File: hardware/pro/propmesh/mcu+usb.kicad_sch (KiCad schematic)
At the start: 14 parts, among them J4 TYPE-C-31-M-12, SW1 TS-1187A, SW2 TS-1187A, U3 ESP32-S3-WROOM-1U-N8R2, U4 USBLC6-2SC6

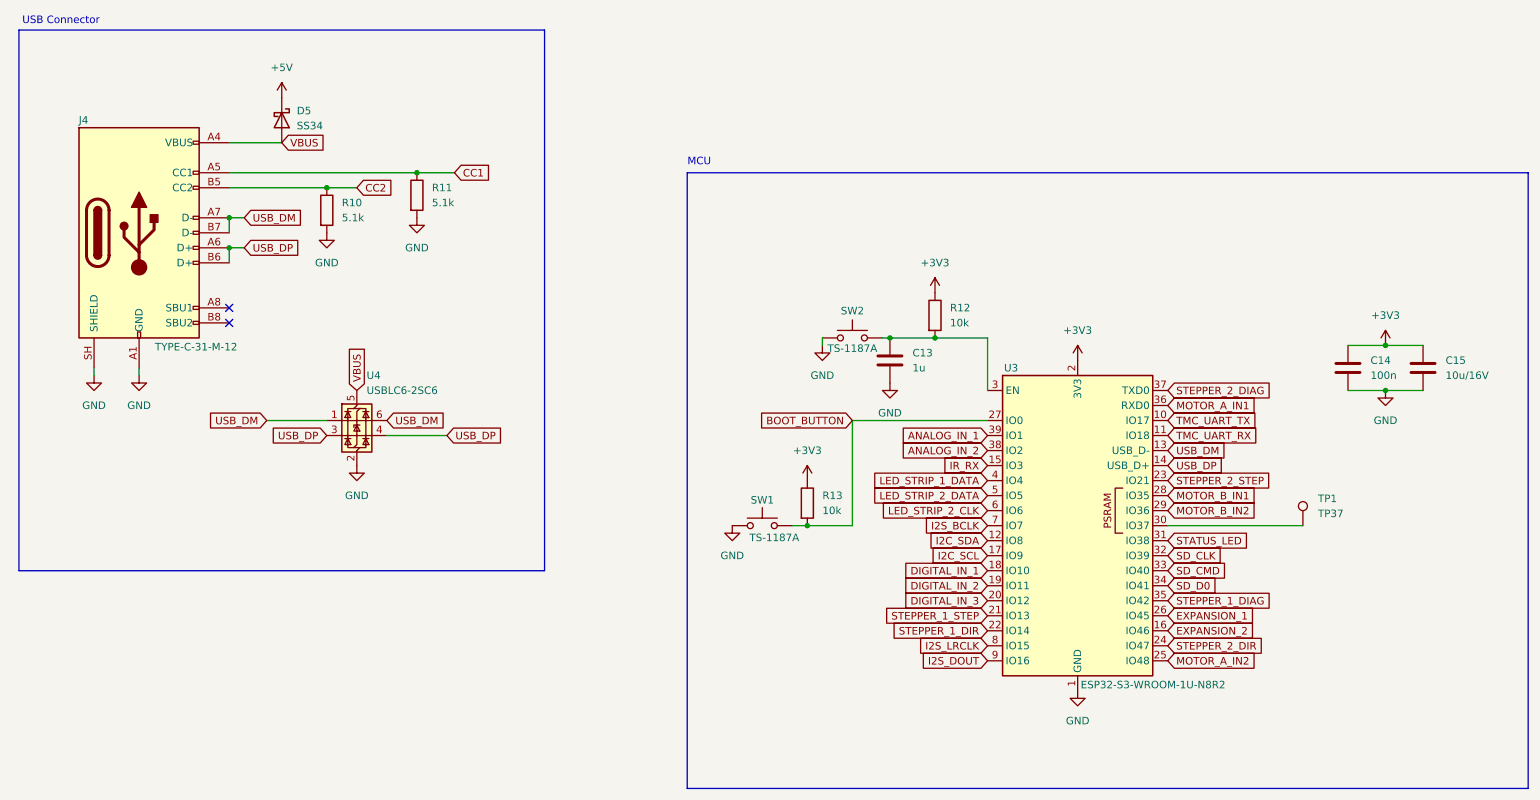
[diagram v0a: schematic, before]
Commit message: Pro schematic complete; enclosure, layout guide, timeline and radio decisions
Schematic: all seven design sheets drawn and green; project-wide ERC at
zero. IR receiver dropped (hidden board can't see a remote — plug-in on
a DIGITAL_IN); GPIO 3 became LED_STRIP_1_CLK; both strip outputs 3- or
4-wire through one octal SN74AHCT541DWR (three revisions of the shifter
in one day, no mode jumpers). Input FET symbol replaced: KiCad 10's
Device:Q_PMOS numbers pins D/G/S and matches no pad — the part would
have been unconnected with no ERC/DRC complaint. All 196 references
renumbered to standard sequential designators (yaml keeps spec names;
the checker prints both). Sheet 08 (test points) and the sheet 01
staged-power link headers specified per spec §2.6 — sheet 01's checker
is red until they are drawn.

checknet.py: symbol pins ⊆ footprint pads check (the silent killer),
multi-unit pin keys + per-unit diagrams (`units:`), symbol-vote sheet
anchoring for half-drawn sheets, orientation-aware net voting, foreign
part reporting, cross-sheet extras no longer crash the report.

Docs: hardware/pro/layout.md — placement by designator, IPC-2221 trace
widths, thermal, silk, ⚠ list, KiCad primer; every chip's datasheet
layout section read (WROOM-1U has NO keep-out; DRV8871 wants a bottom
GND pour; MAX98357A output-trace numbers). Enclosure plan (spec §2.3):
Multilink RNI-1500 / RNI-300, DRiBOX Medium, Joinfworld clear-lid box,
icotek KEL-DPZ entry plate, fit rule 210×140×60 mm inside; PSU
defaults (§2.9) and the 10 A input-path note. Software plan: timeline
design (ramps native, live scrub v1, Cue.start_offset_ms in schema),
yard access (walk-up AP, WireGuard-in-firmware, BYO remote), WiFi-PHY
radio decision vs Zigbee/BLE/LoRa, console served-from-bridge budget,
USB stays in CDC/JTAG mode (no auto-program transistors needed).

Co-Authored-By: Claude Fable 5.1 <noreply@anthropic.com>
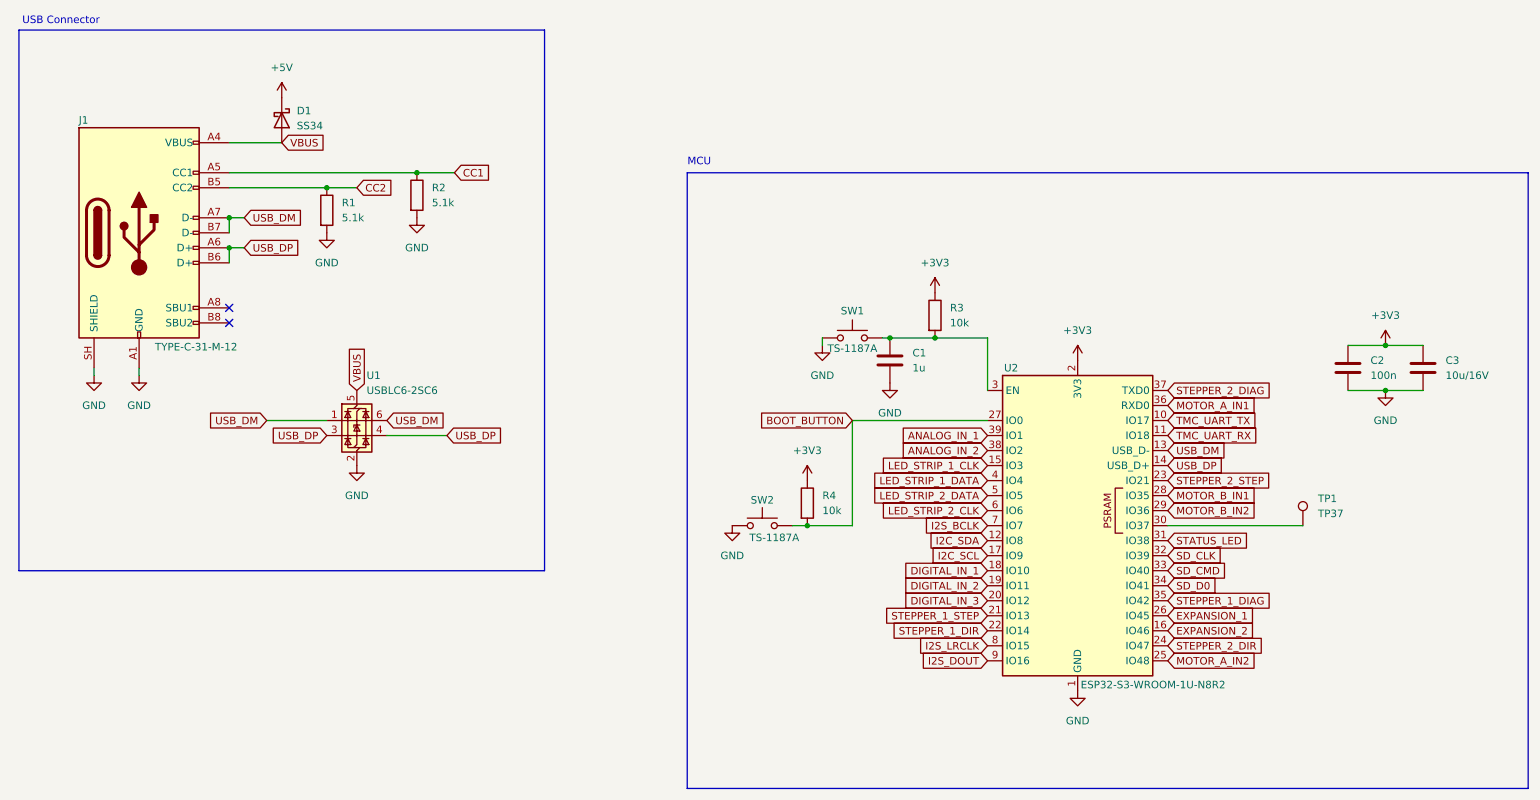
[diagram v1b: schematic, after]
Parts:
- renumbered C13 to C1, C14 to C2, C15 to C3, D5 to D1, J4 to J1, R10 to R1, R11 to R2, R12 to R3, R13 to R4, SW2 to SW1, SW1 to SW2, U4 to U1, U3 to U2
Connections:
- net IR_RX renamed LED_STRIP_1_CLK
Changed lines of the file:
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@@
 		)
 	)
-	(global_label "IR_RX"
+	(global_label "LED_STRIP_1_CLK"
 		(shape input)
 		(at 186.69 93.98 180)
@@
 		)
 		(property "Intersheetrefs" "${INTERSHEET_REFS}"
-			(at 178.3829 93.98 0)
+			(at 167.2554 93.98 0)
 			(hide yes)
 			(show_name no)
@@
 		(dnp no)
 		(fields_autoplaced yes)
-		(property "Reference" "C15"
+		(property "Reference" "C3"
 			(at 264.16 76.1999 0)
 			(show_name no)
@@
 			(project "propmesh"
 				(path "/6aa579d1-bfe0-499b-882d-72f52ff6d36c/0f32bd3b-d69f-46e3-8384-0dd06a686621"
-					(reference "C15")
+					(reference "C3")
 					(unit 1)
 				)
@@
 		(dnp no)
 		(fields_autoplaced yes)
-		(property "Reference" "C13"
+		(property "Reference" "C1"
 			(at 173.99 74.9299 0)
 			(show_name no)
@@
 			(project "propmesh"
 				(path "/6aa579d1-bfe0-499b-882d-72f52ff6d36c/0f32bd3b-d69f-46e3-8384-0dd06a686621"
-					(reference "C13")
+					(reference "C1")
 					(unit 1)
 				)
@@
 		(dnp no)
 		(fields_autoplaced yes)
-		(property "Reference" "#PWR031"
+		(property "Reference" "#PWR030"
 			(at 80.01 100.33 0)
 			(hide yes)
@@
 			(project "propmesh"
 				(path "/6aa579d1-bfe0-499b-882d-72f52ff6d36c/0f32bd3b-d69f-46e3-8384-0dd06a686621"
-					(reference "#PWR031")
+					(reference "#PWR030")
 					(unit 1)
 				)
@@
 		(dnp no)
 		(fields_autoplaced yes)
-		(property "Reference" "#PWR06"
+		(property "Reference" "#PWR031"
 			(at 90.17 58.42 0)
 			(hide yes)
@@
 			(project "propmesh"
 				(path "/6aa579d1-bfe0-499b-882d-72f52ff6d36c/0f32bd3b-d69f-46e3-8384-0dd06a686621"
-					(reference "#PWR06")
+					(reference "#PWR031")
 					(unit 1)
 				)
@@
 		(dnp no)
 		(fields_autoplaced yes)
-		(property "Reference" "C14"
+		(property "Reference" "C2"
 			(at 251.46 76.1999 0)
 			(show_name no)
@@
 			(project "propmesh"
 				(path "/6aa579d1-bfe0-499b-882d-72f52ff6d36c/0f32bd3b-d69f-46e3-8384-0dd06a686621"
-					(reference "C14")
+					(reference "C2")
 					(unit 1)
 				)
@@
 		(dnp no)
 		(fields_autoplaced yes)
-		(property "Reference" "U4"
+		(property "Reference" "U1"
 			(at 81.6611 78.74 0)
 			(show_name no)
@@
 			(project "propmesh"
 				(path "/6aa579d1-bfe0-499b-882d-72f52ff6d36c/0f32bd3b-d69f-46e3-8384-0dd06a686621"
-					(reference "U4")
+					(reference "U1")
 					(unit 1)
 				)
@@
 		(in_pos_files yes)
 		(dnp no)
-		(property "Reference" "J4"
+		(property "Reference" "J1"
 			(at 33.782 35.56 0)
 			(show_name no)
@@
 			(project "propmesh"
 				(path "/6aa579d1-bfe0-499b-882d-72f52ff6d36c/0f32bd3b-d69f-46e3-8384-0dd06a686621"
-					(reference "J4")
+					(reference "J1")
 					(unit 1)
 				)
@@
 		(dnp no)
 		(fields_autoplaced yes)
-		(property "Reference" "R11"
+		(property "Reference" "R2"
 			(at 92.71 46.9899 0)
 			(show_name no)
@@
 			(project "propmesh"
 				(path "/6aa579d1-bfe0-499b-882d-72f52ff6d36c/0f32bd3b-d69f-46e3-8384-0dd06a686621"
-					(reference "R11")
+					(reference "R2")
 					(unit 1)
 				)
@@
 		(dnp no)
 		(fields_autoplaced yes)
-		(property "Reference" "R13"
+		(property "Reference" "R4"
 			(at 158.75 99.0599 0)
 			(show_name no)
@@
 			(project "propmesh"
 				(path "/6aa579d1-bfe0-499b-882d-72f52ff6d36c/0f32bd3b-d69f-46e3-8384-0dd06a686621"
-					(reference "R13")
+					(reference "R4")
 					(unit 1)
 				)
@@
 		(dnp no)
 		(fields_autoplaced yes)
-		(property "Reference" "#PWR036"
+		(property "Reference" "#PWR035"
 			(at 170.18 86.36 0)
 			(hide yes)
@@
 			(project "propmesh"
 				(path "/6aa579d1-bfe0-499b-882d-72f52ff6d36c/0f32bd3b-d69f-46e3-8384-0dd06a686621"
-					(reference "#PWR036")
+					(reference "#PWR035")
 					(unit 1)
 				)
@@
 		(dnp no)
 		(fields_autoplaced yes)
-		(property "Reference" "R10"
+		(property "Reference" "R1"
 			(at 77.47 49.5299 0)
 			(show_name no)
@@
 			(project "propmesh"
 				(path "/6aa579d1-bfe0-499b-882d-72f52ff6d36c/0f32bd3b-d69f-46e3-8384-0dd06a686621"
-					(reference "R10")
+					(reference "R1")
 					(unit 1)
 				)
@@
 		(dnp no)
 		(fields_autoplaced yes)
-		(property "Reference" "#PWR041"
+		(property "Reference" "#PWR026"
 			(at 35.56 85.09 0)
 			(hide yes)
@@
 			(project "propmesh"
 				(path "/6aa579d1-bfe0-499b-882d-72f52ff6d36c/0f32bd3b-d69f-46e3-8384-0dd06a686621"
-					(reference "#PWR041")
+					(reference "#PWR026")
 					(unit 1)
 				)
@@
 		(dnp no)
 		(fields_autoplaced yes)
-		(property "Reference" "#PWR030"
+		(property "Reference" "#PWR027"
 			(at 43.18 85.09 0)
 			(hide yes)
@@
 			(project "propmesh"
 				(path "/6aa579d1-bfe0-499b-882d-72f52ff6d36c/0f32bd3b-d69f-46e3-8384-0dd06a686621"
-					(reference "#PWR030")
+					(reference "#PWR027")
 					(unit 1)
 				)
@@
 		(dnp no)
 		(fields_autoplaced yes)
-		(property "Reference" "#PWR038"
+		(property "Reference" "#PWR036"
 			(at 177.8 68.58 0)
 			(hide yes)
@@
 			(project "propmesh"
 				(path "/6aa579d1-bfe0-499b-882d-72f52ff6d36c/0f32bd3b-d69f-46e3-8384-0dd06a686621"
-					(reference "#PWR038")
+					(reference "#PWR036")
 					(unit 1)
 				)
@@
 		(dnp no)
 		(fields_autoplaced yes)
-		(property "Reference" "R12"
+		(property "Reference" "R3"
 			(at 180.34 67.3099 0)
 			(show_name no)
@@
 			(project "propmesh"
 				(path "/6aa579d1-bfe0-499b-882d-72f52ff6d36c/0f32bd3b-d69f-46e3-8384-0dd06a686621"
-					(reference "R12")
+					(reference "R3")
 					(unit 1)
 				)
@@
 		(dnp no)
 		(fields_autoplaced yes)
-		(property "Reference" "#PWR027"
+		(property "Reference" "#PWR029"
 			(at 74.93 60.96 0)
 			(hide yes)
@@
 			(project "propmesh"
 				(path "/6aa579d1-bfe0-499b-882d-72f52ff6d36c/0f32bd3b-d69f-46e3-8384-0dd06a686621"
-					(reference "#PWR027")
+					(reference "#PWR029")
 					(unit 1)
 				)
@@
 		(dnp no)
 		(fields_autoplaced yes)
-		(property "Reference" "#PWR033"
+		(property "Reference" "#PWR038"
 			(at 201.93 138.43 0)
 			(hide yes)
@@
 			(project "propmesh"
 				(path "/6aa579d1-bfe0-499b-882d-72f52ff6d36c/0f32bd3b-d69f-46e3-8384-0dd06a686621"
-					(reference "#PWR033")
+					(reference "#PWR038")
 					(unit 1)
 				)
@@
 		(dnp no)
 		(fields_autoplaced yes)
-		(property "Reference" "#PWR034"
+		(property "Reference" "#PWR033"
 			(at 156.21 100.33 0)
 			(hide yes)
@@
 			(project "propmesh"
 				(path "/6aa579d1-bfe0-499b-882d-72f52ff6d36c/0f32bd3b-d69f-46e3-8384-0dd06a686621"
-					(reference "#PWR034")
+					(reference "#PWR033")
 					(unit 1)
 				)
@@
 		(dnp no)
 		(fields_autoplaced yes)
-		(property "Reference" "#PWR032"
+		(property "Reference" "#PWR037"
 			(at 201.93 80.01 0)
 			(hide yes)
@@
 			(project "propmesh"
 				(path "/6aa579d1-bfe0-499b-882d-72f52ff6d36c/0f32bd3b-d69f-46e3-8384-0dd06a686621"
-					(reference "#PWR032")
+					(reference "#PWR037")
 					(unit 1)
 				)
@@
 		(in_pos_files yes)
 		(dnp no)
-		(property "Reference" "SW1"
+		(property "Reference" "SW2"
 			(at 148.59 99.822 0)
 			(show_name no)
@@
 			(project "propmesh"
 				(path "/6aa579d1-bfe0-499b-882d-72f52ff6d36c/0f32bd3b-d69f-46e3-8384-0dd06a686621"
-					(reference "SW1")
+					(reference "SW2")
 					(unit 1)
 				)
@@
 		(dnp no)
 		(fields_autoplaced yes)
-		(property "Reference" "#PWR035"
+		(property "Reference" "#PWR032"
 			(at 143.51 110.49 0)
 			(hide yes)
@@
 			(project "propmesh"
 				(path "/6aa579d1-bfe0-499b-882d-72f52ff6d36c/0f32bd3b-d69f-46e3-8384-0dd06a686621"
-					(reference "#PWR035")
+					(reference "#PWR032")
 					(unit 1)
 				)
@@
 		(dnp no)
 		(fields_autoplaced yes)
-		(property "Reference" "#PWR037"
+		(property "Reference" "#PWR034"
 			(at 158.75 80.01 0)
 			(hide yes)
@@
 			(project "propmesh"
 				(path "/6aa579d1-bfe0-499b-882d-72f52ff6d36c/0f32bd3b-d69f-46e3-8384-0dd06a686621"
-					(reference "#PWR037")
+					(reference "#PWR034")
 					(unit 1)
 				)
@@
 		(in_pos_files yes)
 		(dnp no)
-		(property "Reference" "SW2"
+		(property "Reference" "SW1"
 			(at 163.83 67.818 0)
 			(show_name no)
@@
 			(project "propmesh"
 				(path "/6aa579d1-bfe0-499b-882d-72f52ff6d36c/0f32bd3b-d69f-46e3-8384-0dd06a686621"
-					(reference "SW2")
+					(reference "SW1")
 					(unit 1)
 				)
@@
 		(in_pos_files yes)
 		(dnp no)
-		(property "Reference" "U3"
+		(property "Reference" "U2"
 			(at 189.484 77.47 0)
 			(show_name no)
@@
 			(project "propmesh"
 				(path "/6aa579d1-bfe0-499b-882d-72f52ff6d36c/0f32bd3b-d69f-46e3-8384-0dd06a686621"
-					(reference "U3")
+					(reference "U2")
 					(unit 1)
 				)
@@
 		(dnp no)
 		(fields_autoplaced yes)
-		(property "Reference" "D5"
+		(property "Reference" "D1"
 			(at 69.85 33.9724 90)
 			(show_name no)
@@
 			(project "propmesh"
 				(path "/6aa579d1-bfe0-499b-882d-72f52ff6d36c/0f32bd3b-d69f-46e3-8384-0dd06a686621"
-					(reference "D5")
+					(reference "D1")
 					(unit 1)
 				)

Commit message: Pro v0.1 schematic complete; board cleanup pass, parity 0
Schematic: all datasheet-review changes drawn (decisions 1A, 2A, 3B,
OE on GPIO 37, 4B). All eight sheet checkers ALL NETS MATCH, ERC 0
errors / 0 warnings, pinmap matches generated headers.
- sheet 03: second PCA9685 (U12, 0x41) with B-straps, PCA_OE net with
  10k pull-up (R59); DC FETs Q1-Q6 = SI2356DS
- sheets 02/04/05/07/08: USB link/22R/VBUS cap, SD DAT1/DAT2 pull-ups,
  shifter pulldowns, 2.2k 1206 sensor Rs; R53 (GPIO3 pulldown) now drawn
  on sheet 05, specs moved to match

Board (KiCad closed, backup kept):
- F8 done, schematic parity 0; orphan DNP R53 removed
- mounting holes H1-H4, board-only, excluded from BOM/position files
- minimum drill 0.3 -> 0.2 mm: U2's own 0.2/0.6 thermal vias; JLCPCB
  4-layer standard cost for 0.2 mm holes with >= 0.45 mm pads
- DG128-02P pads 2.3 -> 2.8 mm (J17 10 A input; library edited too)
- DRV8871 exposed-pad paste inset 0.1 mm (library edited too)
- 43 parts snapped to grid; snapgrid.py now exempts J20/J22 so the
  StepStick rows stay 12.70 mm
- DRC: 11 courtyard overlaps left (3 accepted terminal gangs, 8 in the
  sensor corner from the 1206 resistors) + silkscreen

Tools: checknet.py net vote ignores orientation for R/C/L (three
upside-down pull-ups had out-voted the chip pin on sheet 04); verified
it still catches a shorted net and a mis-wired pull-up.
checksetup.py: min drill 0.2.

Also includes the Mini module selection and KiCad project started in
another session (2026-09-19).

Co-Authored-By: Claude Opus 5.5 <noreply@anthropic.com>
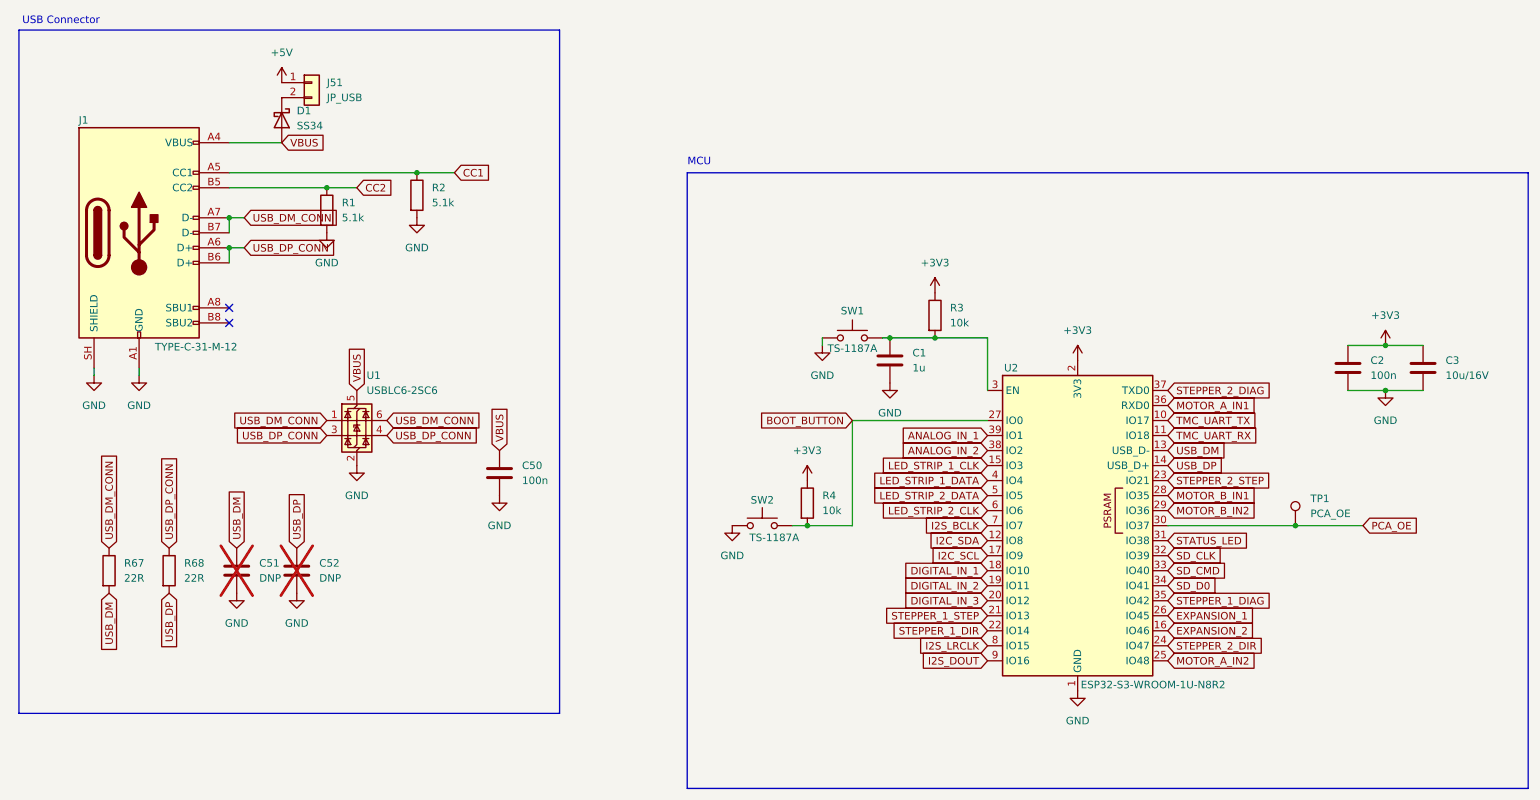
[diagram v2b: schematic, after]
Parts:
- added C50: 100n, Capacitor_SMD:C_0603_1608Metric, symbol Device:C
- added C51, C52: DNP, Capacitor_SMD:C_0603_1608Metric, symbol Device:C
- added J51: JP_USB, Connector_PinHeader_2.54mm:PinHeader_1x02_P2.54mm_Vertical, symbol Connector_Generic:Conn_01x02
- added R67, R68: 22R, Resistor_SMD:R_0603_1608Metric, symbol Device:R
- TP1: value TP37 -> PCA_OE
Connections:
- net +5V: now also J51.1 (Pin_1); no longer D1.1 (K)
- net GND: now also C50.2, C51.2, C52.2
- net USB_DM: now also C51.1, R67.2; no longer J1.A7 (D-), J1.B7 (D-), U1.1 (I/O1), U1.6 (I/O1)
- net USB_DP: now also C52.1, R68.2; no longer J1.A6 (D+), J1.B6 (D+), U1.3 (I/O2), U1.4 (I/O2)
- net VBUS: now also C50.1
- net PCA_OE: now reaches TP1.1, U2.30 (IO37)
- new net: D1.1 (K), J51.2 (Pin_2)
- new net USB_DM_CONN: J1.A7 (D-), J1.B7 (D-), R67.1, U1.1 (I/O1), U1.6 (I/O1)
- new net USB_DP_CONN: J1.A6 (D+), J1.B6 (D+), R68.1, U1.3 (I/O2), U1.4 (I/O2)
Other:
- moved on the sheet: TP1
